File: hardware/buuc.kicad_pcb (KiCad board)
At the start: 2 copper layers, 45.1 x 29.8 mm, 18 parts, among them P1 USB_OTG, P2 CONN_01X02, Q1 NDS8434, U1 BOOST_REGULATOR, U2 MCP73842-840I/UN, U3 MIC2005A

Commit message: Apparently: active low.  FFS.
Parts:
- moved R6 3.59 mm to (54.6, 48.3)
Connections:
- R6 pad 1: Net-(C4-Pad2) -> GND
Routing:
- net GND: track 22.7 -> 25.2 mm
- net Net-(R6-Pad2): track 7.12 -> 6.06 mm
- net Net-(C4-Pad2): track 19.0 -> 18.2 mm
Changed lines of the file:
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@@
   )
   (module coddingtonbear/coddingtonbear.pretty:0805_Milling (layer F.Cu)
-    (at 57.15 45.72 180)
+    (at 54.61 48.26 180)
     (descr "Resistor SMD 0805, reflow soldering, Vishay (see dcrcw.pdf)")
     (tags "resistor 0805")
@@
       (net 18 "Net-(R6-Pad2)"))
     (pad 1 smd rect (at -1 0 180) (size 1.8 1.3) (layers F.Cu F.Paste F.Mask)
-      (net 17 "Net-(C4-Pad2)"))
+      (net 2 GND))
     (model Resistors_SMD.3dshapes/R_0805.wrl
       (at (xyz 0 0 0))
@@
   (segment (start 85.48 38.735) (end 83.185 38.735) (width 0.5) (layer F.Cu) (net 1))
   (segment (start 83.185 38.735) (end 81.57464 38.735) (width 0.5) (layer F.Cu) (net 1))
+  (segment (start 55.61 48.26) (end 58.055 48.26) (width 0.45) (layer F.Cu) (net 2) (status C00000))
   (segment (start 56.54294 39.04996) (end 56.54294 40.03294) (width 0.35) (layer F.Cu) (net 2))
   (via (at 59.055 41.275) (size 1.5) (drill 0.5) (layers F.Cu B.Cu) (net 2))
@@
   (segment (start 70.825 43.555) (end 71.2 43.18) (width 0.25) (layer F.Cu) (net 16))
   (segment (start 72.945 43.18) (end 71.2 43.18) (width 0.5) (layer F.Cu) (net 16))
-  (segment (start 53.94706 39.04996) (end 53.94706 41.88206) (width 0.35) (layer F.Cu) (net 17))
-  (segment (start 58.5 44.53) (end 57.785 43.815) (width 0.45) (layer F.Cu) (net 17))
-  (segment (start 57.785 43.815) (end 55.88 43.815) (width 0.45) (layer F.Cu) (net 17))
-  (segment (start 58.5 44.53) (end 58.5 45.72) (width 0.45) (layer F.Cu) (net 17))
-  (segment (start 53.94706 41.88206) (end 55.88 43.815) (width 0.35) (layer F.Cu) (net 17))
+  (segment (start 53.94706 39.04996) (end 53.94706 41.24706) (width 0.35) (layer F.Cu) (net 17) (status 400000))
+  (segment (start 55.245 42.545) (end 53.975 41.275) (width 0.45) (layer F.Cu) (net 17))
+  (segment (start 60.055 45.45) (end 57.15 42.545) (width 0.45) (layer F.Cu) (net 17))
+  (segment (start 60.055 45.45) (end 60.055 48.26) (width 0.45) (layer F.Cu) (net 17) (status 800000))
+  (segment (start 57.15 42.545) (end 55.245 42.545) (width 0.45) (layer F.Cu) (net 17))
+  (segment (start 53.94706 41.24706) (end 53.975 41.275) (width 0.35) (layer F.Cu) (net 17))
+  (segment (start 53.975 39.0779) (end 53.94706 39.04996) (width 0.35) (layer F.Cu) (net 17) (status C00000))
   (segment (start 60.305 48.26) (end 60.305 50.47) (width 0.45) (layer F.Cu) (net 17))
   (segment (start 60.305 50.47) (end 58.1 52.675) (width 0.45) (layer F.Cu) (net 17))
-  (segment (start 58.5 45.72) (end 59.69 45.72) (width 0.45) (layer F.Cu) (net 17))
-  (segment (start 60.305 46.335) (end 60.305 48.26) (width 0.45) (layer F.Cu) (net 17))
-  (segment (start 59.69 45.72) (end 60.305 46.335) (width 0.45) (layer F.Cu) (net 17))
-  (segment (start 56.2 52.675) (end 56.2 51.755) (width 0.45) (layer F.Cu) (net 18))
-  (segment (start 55.8 51.355) (end 55.8 45.72) (width 0.45) (layer F.Cu) (net 18))
-  (segment (start 56.2 51.755) (end 55.8 51.355) (width 0.45) (layer F.Cu) (net 18))
+  (segment (start 56.2 52.675) (end 55.215 52.675) (width 0.45) (layer F.Cu) (net 18) (status 400000))
+  (segment (start 53.61 51.07) (end 53.61 48.26) (width 0.45) (layer F.Cu) (net 18) (status 800000))
+  (segment (start 55.215 52.675) (end 53.61 51.07) (width 0.45) (layer F.Cu) (net 18))
   (zone (net 2) (net_name GND) (layer B.Cu) (hatch edge 0.508)
     (connect_pads (clearance 1))

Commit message: Adding extra pads allowing me to fine-tune the consumed current; adding unpopulated bypass resistor around the MIC2005.
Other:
- net class Default: trace_width 0.45 -> 0.25
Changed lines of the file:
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@@
-(kicad_pcb (version 20160815) (host pcbnew "(2016-12-18 revision 3ffa37c)-master")
+(kicad_pcb (version 20170123) (host pcbnew no-vcs-found-e2505cb~60~ubuntu16.04.1)
   (general
-    (links 39)
-    (no_connects 0)
-    (area 46.914999 34.214999 92.150001 64.210001)
     (thickness 1.6)
-    (drawings 8)
+    (drawings 4)
     (tracks 121)
     (zones 0)
@@
   )
   (setup
-    (last_trace_width 0.35)
+    (last_trace_width 0.25)
     (user_trace_width 0.25)
     (user_trace_width 0.35)
@@
     (pad_drill 0.762)
     (pad_to_mask_clearance 0.2)
-    (aux_axis_origin 135.255 81.915)
+    (aux_axis_origin 46.99 64.008)
     (visible_elements FFFFFF7F)
     (pcbplotparams
-      (layerselection 0x000c0_ffffffff)
+      (layerselection 0x01000_ffffffff)
       (usegerberextensions false)
       (usegerberattributes true)
       (usegerberadvancedattributes true)
+      (creategerberjobfile true)
       (excludeedgelayer true)
       (linewidth 0.100000)
@@
   (net_class Default "This is the default net class."
     (clearance 0.2)
-    (trace_width 0.45)
+    (trace_width 0.25)
     (via_dia 1.5)
     (via_drill 0.5)
     (uvia_dia 0.3)
     (uvia_drill 0.1)
-    (diff_pair_gap 0.25)
-    (diff_pair_width 0.2)
     (add_net +5V)
     (add_net +BATT)
@@
     )
   )
-  (target plus (at 93.345 33.02) (size 5) (width 0.15) (layer Edge.Cuts))
-  (target x (at 79.375 66.675) (size 5) (width 0.15) (layer Edge.Cuts))
-  (target plus (at 45.72 65.405) (size 5) (width 0.15) (layer Edge.Cuts))
-  (target plus (at 45.72 33.02) (size 5) (width 0.15) (layer Edge.Cuts))
   (gr_line (start 46.99 64.135) (end 46.99 34.29) (angle 90) (layer Edge.Cuts) (width 0.15))
   (gr_line (start 92.075 64.135) (end 46.99 64.135) (angle 90) (layer Edge.Cuts) (width 0.15))

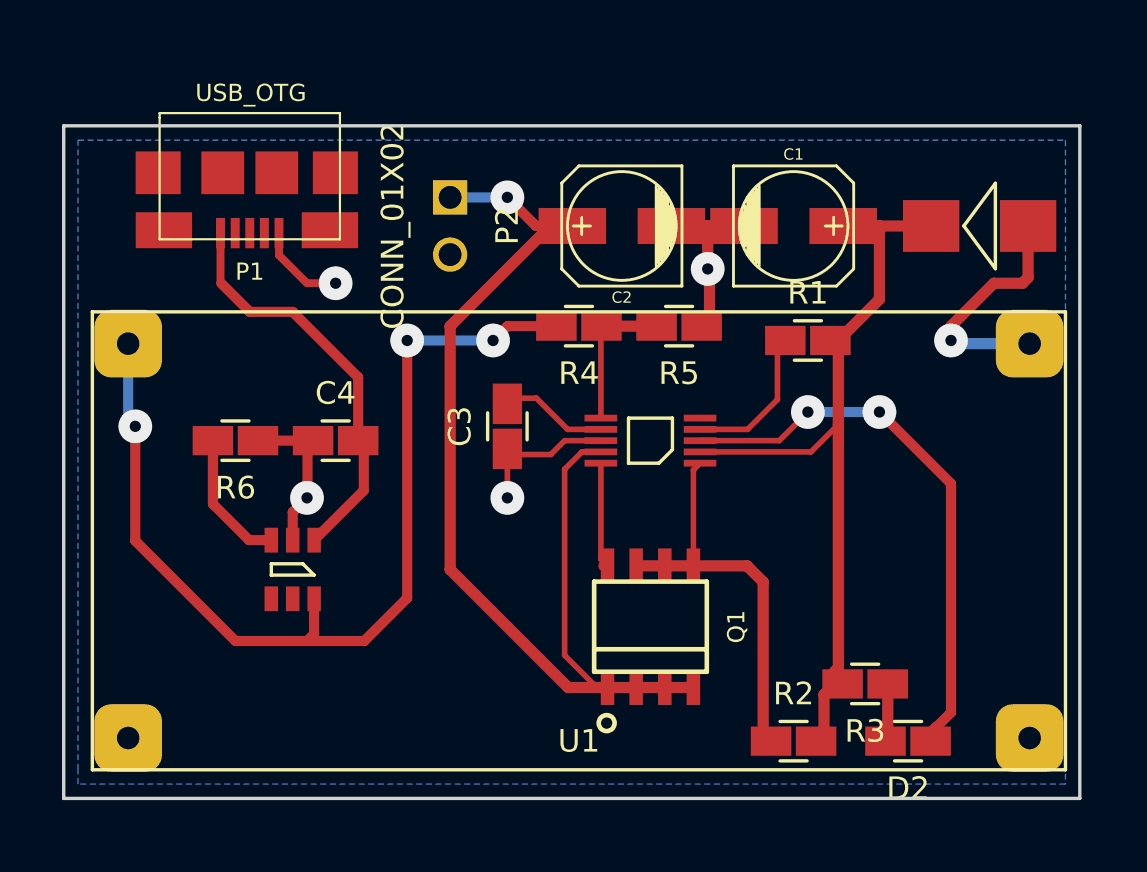
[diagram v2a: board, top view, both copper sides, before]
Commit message: Updating to use a grid of current sense resistors for configurability.
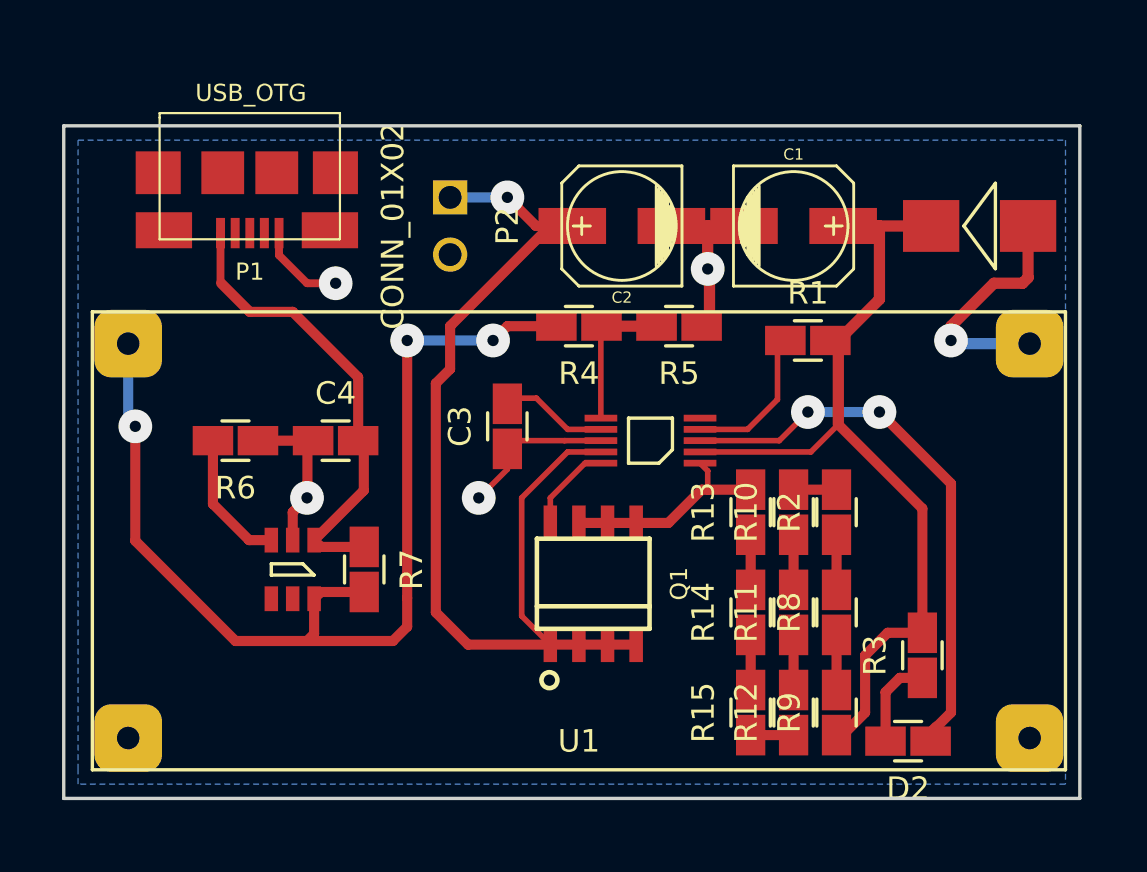
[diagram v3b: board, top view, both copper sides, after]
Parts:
- added R10: 0, coddingtonbear/coddingtonbear.pretty:0805_Milling, F.Cu at (79.4, 51.4)
- added R11: 0, coddingtonbear/coddingtonbear.pretty:0805_Milling, F.Cu at (79.4, 55.9)
- added R12: 0, coddingtonbear/coddingtonbear.pretty:0805_Milling, F.Cu at (79.4, 60.3)
- added R13: 0, coddingtonbear/coddingtonbear.pretty:0805_Milling, F.Cu at (77.5, 51.4)
- added R14: 0, coddingtonbear/coddingtonbear.pretty:0805_Milling, F.Cu at (77.5, 55.9)
- added R15: 0, coddingtonbear/coddingtonbear.pretty:0805_Milling, F.Cu at (77.5, 60.3)
- added R7: EMPTY, coddingtonbear/coddingtonbear.pretty:0805_Milling, F.Cu at (60.3, 54.0)
- added R8: 0, coddingtonbear/coddingtonbear.pretty:0805_Milling, F.Cu at (81.3, 55.9)
- added R9: 100m, coddingtonbear/coddingtonbear.pretty:0805_Milling, F.Cu at (81.3, 60.3)
- R2: value 100m -> 0
- moved R2 10.3 mm to (81.3, 51.4), turned to 90 degrees
- moved Q1 3.18 mm to (70.5, 54.6)
- moved R3 2.84 mm to (85.1, 57.8), turned to 90 degrees
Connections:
- R2 pad 1: Net-(Q1-Pad3) -> Net-(R2-Pad1)
- R2 pad 2: Net-(C1-Pad1) -> Net-(R10-Pad2)
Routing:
- net Net-(Q1-Pad3): track 17.7 -> 9.55 mm
- net +5V: track 43.5 -> 46.6 mm
- net Net-(C1-Pad1): track 35.1 -> 38.1 mm
- net Net-(R8-Pad1): track 0.00 -> 2.45 mm
- net Net-(R2-Pad1): track 0.00 -> 2.45 mm
- net Net-(R14-Pad1): track 0.00 -> 2.45 mm
- net Net-(R13-Pad1): track 0.00 -> 2.45 mm
- net Net-(R11-Pad1): track 0.00 -> 2.45 mm
- net Net-(R10-Pad1): track 0.00 -> 2.45 mm
- net Net-(C4-Pad2): track 18.2 -> 20.6 mm
- net Net-(R12-Pad1): track 0.00 -> 1.91 mm
- net Net-(R10-Pad2): track 0.00 -> 1.91 mm
- net +BATT: track 50.6 -> 49.0 mm
- net Net-(D2-Pad2): track 3.17 -> 4.56 mm
- net Net-(Q1-Pad1): track 4.84 -> 3.99 mm
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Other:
- net class Default: trace_width 0.25 -> 0.45

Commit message: Switch to through-hole USB adapter; the SMD component is a little too jiggly, and I don't have better ones on-hand at the moment.
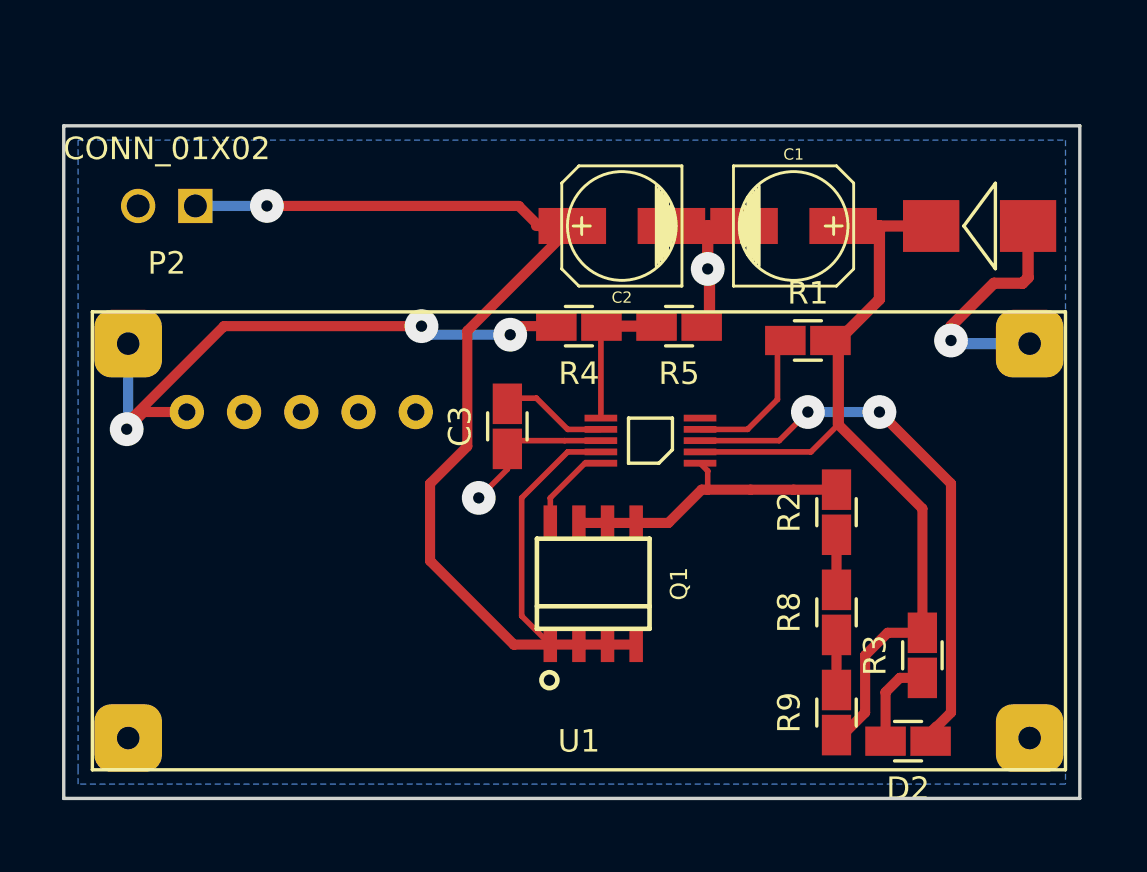
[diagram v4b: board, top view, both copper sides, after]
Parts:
- removed C4: 0.1u, coddingtonbear/coddingtonbear.pretty:0805_Milling
- removed R10, R11, R12, R13, R14, R15: 0, coddingtonbear/coddingtonbear.pretty:0805_Milling
- removed R6: 10k, coddingtonbear/coddingtonbear.pretty:0805_Milling
- removed R7: EMPTY, coddingtonbear/coddingtonbear.pretty:0805_Milling
- removed U3: MIC2005A, adamgreig/agg-kicad/agg.pretty:SOT-23-6
- P1: footprint coddingtonbear/coddingtonbear.pretty:MICRO-B_USB-INVERTED -> coddingtonbear/coddingtonbear.pretty:USB_Thru_hole; moved to B.Cu
- R2, R8: value 0 -> 100m
- moved P2 12.6 mm to (51.6, 37.8), turned to 180 degrees
- moved P1 12.3 mm to (57.5, 47.0)
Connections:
- P1 pad 1: Net-(C4-Pad2) -> +5V
- R2 pad 2: Net-(R10-Pad2) -> Net-(Q1-Pad3)
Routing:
- net Net-(C4-Pad2): track 20.6 -> 0.00 mm
- net +5V: track 46.6 -> 28.2 mm
- net +BATT: track 49.0 -> 61.2 mm
- net GND: track 25.8 -> 14.7 mm, vias 4 -> 2
- net Net-(R6-Pad2): track 6.06 -> 0.00 mm
- net Net-(Q1-Pad3): track 9.55 -> 13.4 mm
- net Net-(R14-Pad1): track 2.45 -> 0.00 mm
- net Net-(R13-Pad1): track 2.45 -> 0.00 mm
- net Net-(R11-Pad1): track 2.45 -> 0.00 mm
- net Net-(R10-Pad1): track 2.45 -> 0.00 mm
- net Net-(R12-Pad1): track 1.91 -> 0.00 mm
- net Net-(R10-Pad2): track 1.91 -> 0.00 mm

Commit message: If I'm going to do this another time, I might as well make it count.
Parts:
- removed P2: CONN_01X02, myelin/myelin-kicad.pretty:header_01x02_40mil_60mil
- added J1: RADIO+, coddingtonbear/coddingtonbear.pretty:TAB, F.Cu at (71.6, 37.6)
- added J2: RADIO-, coddingtonbear/coddingtonbear.pretty:TAB, F.Cu at (85.3, 37.6)
- C1, C2: value 10u -> 22uF; footprint pelrun/libKiCad/footprint/w_smd_cap.pretty:c_elec_5x5.8 -> KiCad/Capacitors_SMD.pretty:C_1206_HandSoldering
- P1: footprint coddingtonbear/coddingtonbear.pretty:USB_Thru_hole -> coddingtonbear/coddingtonbear.pretty:UJ2-MIBH-4-SMT; moved to F.Cu
- moved C1 20.4 mm to (76.2, 58.9), turned to 90 degrees
- moved C2 19.1 mm to (64.5, 56.4), turned to 90 degrees
- moved D1 14.2 mm to (89.4, 52.8), turned to 90 degrees
- moved R2 2.07 mm to (79.2, 51.8)
- moved R9 2.07 mm to (79.2, 59.9)
- moved R8 2.03 mm to (79.2, 55.9)
- moved R3 1.33 mm to (83.8, 57.4)
- moved P1 1.33 mm to (57.1, 45.7)
- moved D2 1.15 mm to (83.3, 61.5)
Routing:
- net Net-(C1-Pad1): track 38.1 -> 46.9 mm
- net +BATT: track 61.2 -> 52.5 mm, vias 1 -> 0
- net GND: track 14.7 -> 22.5 mm, vias 2 -> 4
- net +5V: track 28.2 -> 35.0 mm
- net VCC: track 10.5 -> 6.91 mm
- net Net-(Q1-Pad3): track 13.4 -> 14.5 mm
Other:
- net class Default: trace_width 0.45 -> 0.25
- board text added: "@coddingtonbear 1 October 2017"
- board text added: "GND"
- board text added: "VCC"

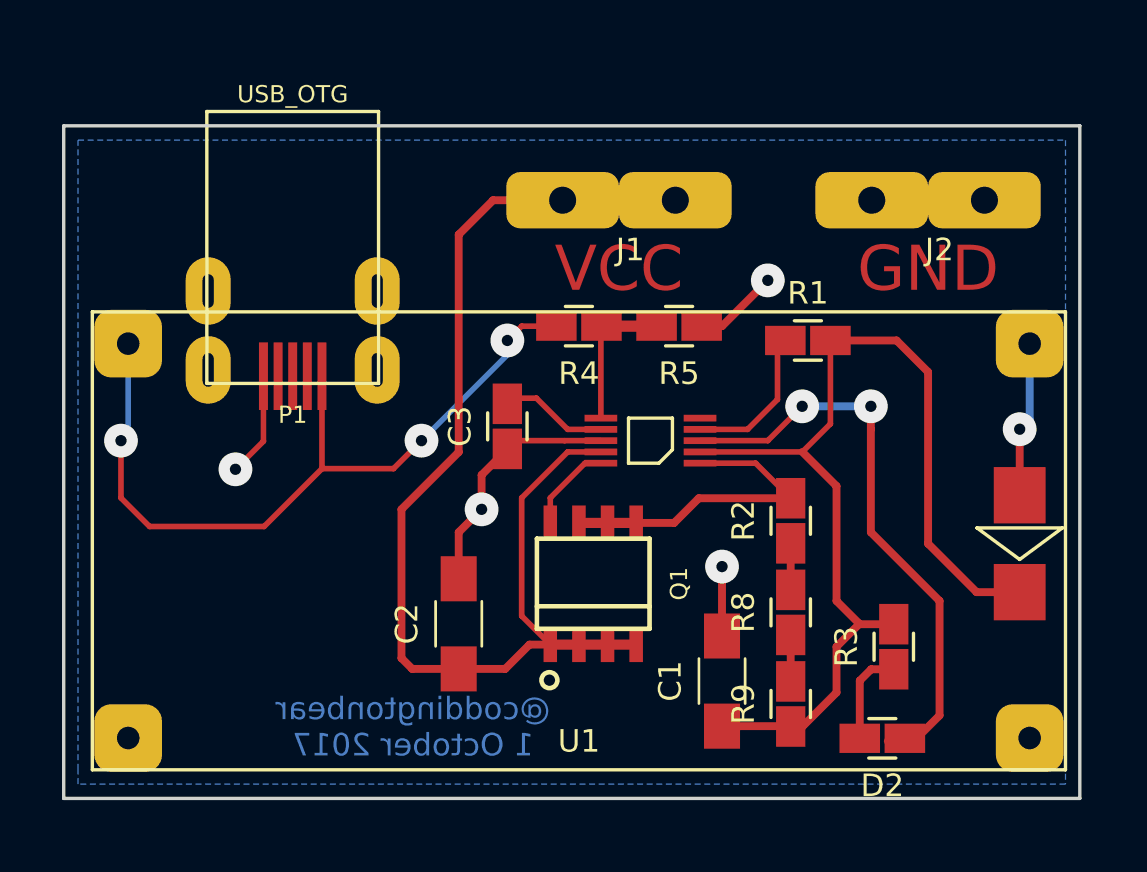
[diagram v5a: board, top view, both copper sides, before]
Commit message: Slightly more compact.
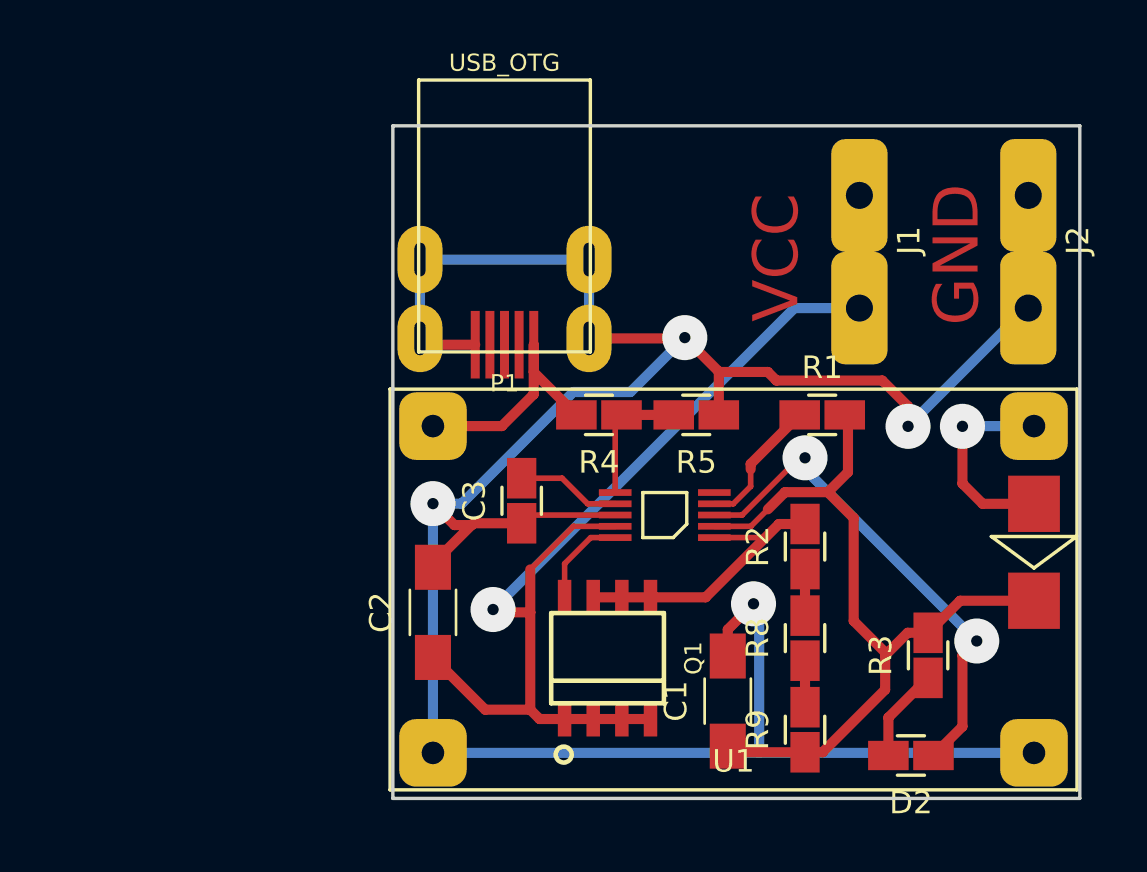
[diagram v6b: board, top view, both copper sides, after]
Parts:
- U1: footprint coddingtonbear/coddingtonbear.pretty:BOOST_REGULATOR -> coddingtonbear/coddingtonbear.pretty:BOOST_TP4056_2A
- moved J1 10.9 mm to (82.3, 39.9), turned to 90 degrees
- moved P1 9.50 mm to (66.5, 44.3)
- moved U1 7.19 mm to (76.7, 54.9)
- moved J2 5.00 mm to (89.8, 39.9), turned to 90 degrees
- moved R4 4.04 mm to (70.7, 47.1)
- moved R5 4.01 mm to (75.1, 47.1)
- moved C3 3.36 mm to (67.3, 50.9)
- moved Q1 3.36 mm to (71.1, 57.9)
- moved R1 3.36 mm to (80.6, 47.1)
- moved U2 3.36 mm to (73.7, 51.6)
- moved R3 1.57 mm to (85.3, 57.8)
- moved D2 1.48 mm to (84.6, 62.2)
- moved R2 1.31 mm to (79.9, 53.0)
- moved R8 1.31 mm to (79.9, 57.0)
- moved R9 1.31 mm to (79.9, 61.1)
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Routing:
- net GND: track 22.5 -> 120.6 mm
- net +5V: track 35.0 -> 11.2 mm, vias 3 -> 0
- net Net-(C1-Pad1): track 46.9 -> 35.2 mm
- net Net-(D2-Pad1): track 25.6 -> 22.3 mm
- net +BATT: track 52.5 -> 50.1 mm, vias 0 -> 1
- net VCC: track 6.91 -> 9.27 mm
- net Net-(Q1-Pad3): track 14.5 -> 15.5 mm
- net Net-(R1-Pad1): track 6.60 -> 6.00 mm
- removed copper zone on B.Cu, net GND
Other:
- board size 45.1 x 29.8 mm -> 30.5 x 29.8 mm
- net class Default: trace_width 0.25 -> 0.45; via_dia 1.5 -> 2
- board text removed: "@coddingtonbear 1 October 2017"
